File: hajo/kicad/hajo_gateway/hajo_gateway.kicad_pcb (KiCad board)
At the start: 2 copper layers, 62 x 92 mm, 20 parts, among them J1 Seetalk NG, J2 WitMtoion, U1 MCP2562, U2 LF50, U3 WeMos_S2_mini, U4 LF33, U5 MAX3232

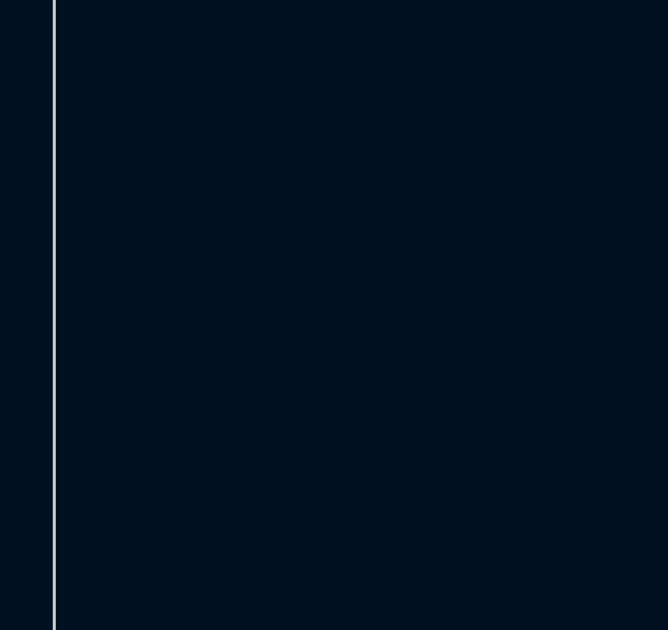
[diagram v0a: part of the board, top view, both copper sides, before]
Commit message: add actisense header
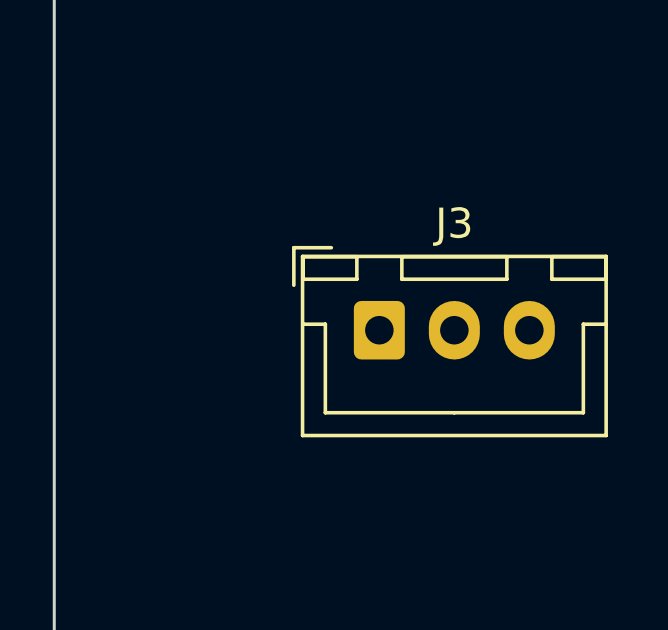
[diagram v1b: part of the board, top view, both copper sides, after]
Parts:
- added J3: Actisense, Connector_JST:JST_XH_B3B-XH-A_1x03_P2.50mm_Vertical, F.Cu at (92.8, 91.2)
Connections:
- U3 pad 15: unconnected-(U3-GPIO37-Pad15) -> /Actisense_TX
- U3 pad 31: unconnected-(U3-GPIO38-Pad31) -> /Actisense_RX

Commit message: redesign gateway pcb
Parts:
- removed C2, C6: 100n, Capacitor_THT:C_Rect_L7.0mm_W2.0mm_P5.00mm
- added JP1: Actisense GND, Connector_PinHeader_2.54mm:PinHeader_1x02_P2.54mm_Vertical, F.Cu at (48.7, 75.9)
- moved J3 56.3 mm to (41.6, 68.1), turned to -90 degrees
- moved U1 23.8 mm to (63.8, 83.9)
- moved U4 15.7 mm to (57.8, 106.6), turned to 90 degrees
- moved J1 13.0 mm to (41.1, 81.3)
- moved C4 10.9 mm to (35.2, 107.5), turned to 90 degrees
- moved U2 10.0 mm to (40.8, 101.5), turned to -90 degrees
- moved C7 8.21 mm to (63.0, 100.7)
- moved J2 7.83 mm to (41.1, 52.6)
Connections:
- J1 pad 2: GND -> /CANH
- J1 pad 3: /CANH -> /CANL
- J1 pad 4: /CANL -> GND
- J3 pad 3: GND -> Net-(J3-Pin_3)
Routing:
- net /Actisense_TX: track 0.00 -> 48.9 mm
- net /Actisense_RX: track 0.00 -> 45.5 mm
- net +3.3V: track 48.6 -> 68.6 mm
- net /CANH: track 11.1 -> 28.4 mm
- net /CANL: track 14.7 -> 32.0 mm
- net +5V: track 137.1 -> 152.2 mm
- net /CanTx: track 44.1 -> 31.9 mm
- net GND: track 237.9 -> 247.4 mm
- net /CanRx: track 39.1 -> 29.8 mm
- net +12V: track 31.3 -> 22.7 mm
- net Net-(J3-Pin_3): track 0.00 -> 7.01 mm
- net Net-(U5-C1-): track 10.7 -> 6.39 mm
- net /RS232_TX: track 30.4 -> 28.3 mm
- net /RS232_RX: track 30.4 -> 28.3 mm
- net Net-(U5-VS-): track 7.99 -> 9.44 mm
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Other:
- outline, holes or cut-outs redrawn
- board text added: "5V"

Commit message: redesign akku pcb
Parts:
- JP1: value Actisense GND -> GND; footprint Connector_PinHeader_2.54mm:PinHeader_1x02_P2.54mm_Vertical -> Connector_PinHeader_2.54mm:PinHeader_1x03_P2.54mm_Vertical
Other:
- board text added: "NC"
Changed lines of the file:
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@@
 		(grid_origin 13 13)
 		(pcbplotparams
-			(layerselection 0x00010fc_ffffffff)
+			(layerselection 0x00010f0_ffffffff)
 			(plot_on_all_layers_selection 0x0000000_00000000)
 			(disableapertmacros no)
@@
 		(tags "connector JST XA vertical")
 		(property "Reference" "J1"
-			(at -1.27 -4.4 90)
+			(at -1.27 -4.572 90)
 			(layer "F.SilkS")
 			(effects
@@
 		)
 		(property "Value" "Seetalk NG"
-			(at 4.706 -4.572 90)
+			(at 6.23 -4.826 90)
 			(layer "F.SilkS")
 			(effects
@@
 			(net 6 "GND")
 			(pinfunction "GND")
-			(pintype "passive")
+			(pintype "power_in")
 		)
 		(pad "27" thru_hole circle
@@
 		)
 		(property "Value" "WitMtoion"
-			(at 6.738 -5.08 90)
+			(at 6.611 -4.953 90)
 			(layer "F.SilkS")
 			(effects
@@
 		)
 	)
-	(footprint "Connector_PinHeader_2.54mm:PinHeader_1x02_P2.54mm_Vertical"
+	(footprint "Connector_PinHeader_2.54mm:PinHeader_1x03_P2.54mm_Vertical"
 		(layer "F.Cu")
 		(at 48.687 75.865 180)
-		(descr "Through hole straight pin header, 1x02, 2.54mm pitch, single row")
-		(tags "Through hole pin header THT 1x02 2.54mm single row")
+		(descr "Through hole straight pin header, 1x03, 2.54mm pitch, single row")
+		(tags "Through hole pin header THT 1x03 2.54mm single row")
 		(property "Reference" "JP1"
-			(at 0 -2.33 360)
+			(at 0 -2.33 180)
 			(layer "F.SilkS")
+			(hide yes)
 			(effects
 				(font
@@
 			)
 		)
-		(property "Value" "Actisense GND"
-			(at -2.794 1.27 90)
+		(property "Value" "GND"
+			(at -3.429 0 180)
 			(layer "F.SilkS")
 			(effects
@@
 			)
 		)
-		(property "Footprint" "Connector_PinHeader_2.54mm:PinHeader_1x02_P2.54mm_Vertical"
+		(property "Footprint" "Connector_PinHeader_2.54mm:PinHeader_1x03_P2.54mm_Vertical"
 			(at 0 0 180)
 			(unlocked yes)
@@
 		(fp_line
 			(start 1.33 1.27)
-			(end 1.33 3.87)
+			(end 1.33 6.41)
 			(stroke
 				(width 0.12)
@@
 		)
 		(fp_line
-			(start -1.33 3.87)
-			(end 1.33 3.87)
+			(start -1.33 6.41)
+			(end 1.33 6.41)
 			(stroke
 				(width 0.12)
@@
 		(fp_line
 			(start -1.33 1.27)
-			(end -1.33 3.87)
+			(end -1.33 6.41)
 			(stroke
 				(width 0.12)
@@
 		)
 		(fp_line
-			(start 1.8 4.35)
+			(start 1.8 6.85)
 			(end 1.8 -1.8)
 			(stroke
@@
 		)
 		(fp_line
-			(start -1.8 4.35)
-			(end 1.8 4.35)
+			(start -1.8 6.85)
+			(end 1.8 6.85)
 			(stroke
 				(width 0.05)
@@
 		(fp_line
 			(start -1.8 -1.8)
-			(end -1.8 4.35)
+			(end -1.8 6.85)
 			(stroke
 				(width 0.05)
@@
 		)
 		(fp_line
-			(start 1.27 3.81)
-			(end -1.27 3.81)
+			(start 1.27 6.35)
+			(end -1.27 6.35)
 			(stroke
 				(width 0.1)
@@
 		(fp_line
 			(start 1.27 -1.27)
-			(end 1.27 3.81)
+			(end 1.27 6.35)
 			(stroke
 				(width 0.1)
@@
 		)
 		(fp_line
-			(start -1.27 3.81)
+			(start -1.27 6.35)
 			(end -1.27 -0.635)
 			(stroke
@@
 		)
 		(fp_text user "${REFERENCE}"
-			(at 0 1.27 90)
+			(at 0 2.54 -90)
 			(layer "F.Fab")
 			(effects
@@
 			(pintype "passive")
 		)
-		(model "${KICAD8_3DMODEL_DIR}/Connector_PinHeader_2.54mm.3dshapes/PinHeader_1x02_P2.54mm_Vertical.wrl"
+		(pad "3" thru_hole oval
+			(at 0 5.08 180)
+			(size 1.7 1.7)
+			(drill 1)
+			(layers "*.Cu" "*.Mask")
+			(remove_unused_layers no)
+		)
+		(model "${KICAD8_3DMODEL_DIR}/Connector_PinHeader_2.54mm.3dshapes/PinHeader_1x03_P2.54mm_Vertical.wrl"
 			(offset
 				(xyz 0 0 0)
@@
 		(layer "F.SilkS")
 		(effects
+			(font
+				(size 1 1)
+				(thickness 0.15)
+			)
+			(justify left bottom)
+		)
+	)
+	(gr_text "NC"
+		(at 50.465 71.293 0)
+		(layer "F.SilkS")
+		(effects

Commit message: fix pcb
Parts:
- moved C5 2.46 mm to (34.3, 45.2), turned to 90 degrees
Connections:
- C5 pad 1: Net-(U5-VS-) -> GND
- C5 pad 2: GND -> Net-(U5-VS-)

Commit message: fix gateway pcb
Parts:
- added JP2: +5V from ESP, Connector_PinHeader_2.54mm:PinHeader_1x02_P2.54mm_Vertical, F.Cu at (68.9, 94.4)
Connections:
- U3 pad 9: unconnected-(U3-VBUS-Pad9) -> Net-(JP2-B)
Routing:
- net Net-(JP2-B): track 0.00 -> 35.3 mm
- net /CanRx: track 29.8 -> 30.8 mm
